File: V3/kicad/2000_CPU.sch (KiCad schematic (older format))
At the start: 21 parts, among them U2100 Z8-L180-S180-180-PQFP-80, U2101 GAL16V8, U2102 14.7456 MHz, U2103 74HCT273

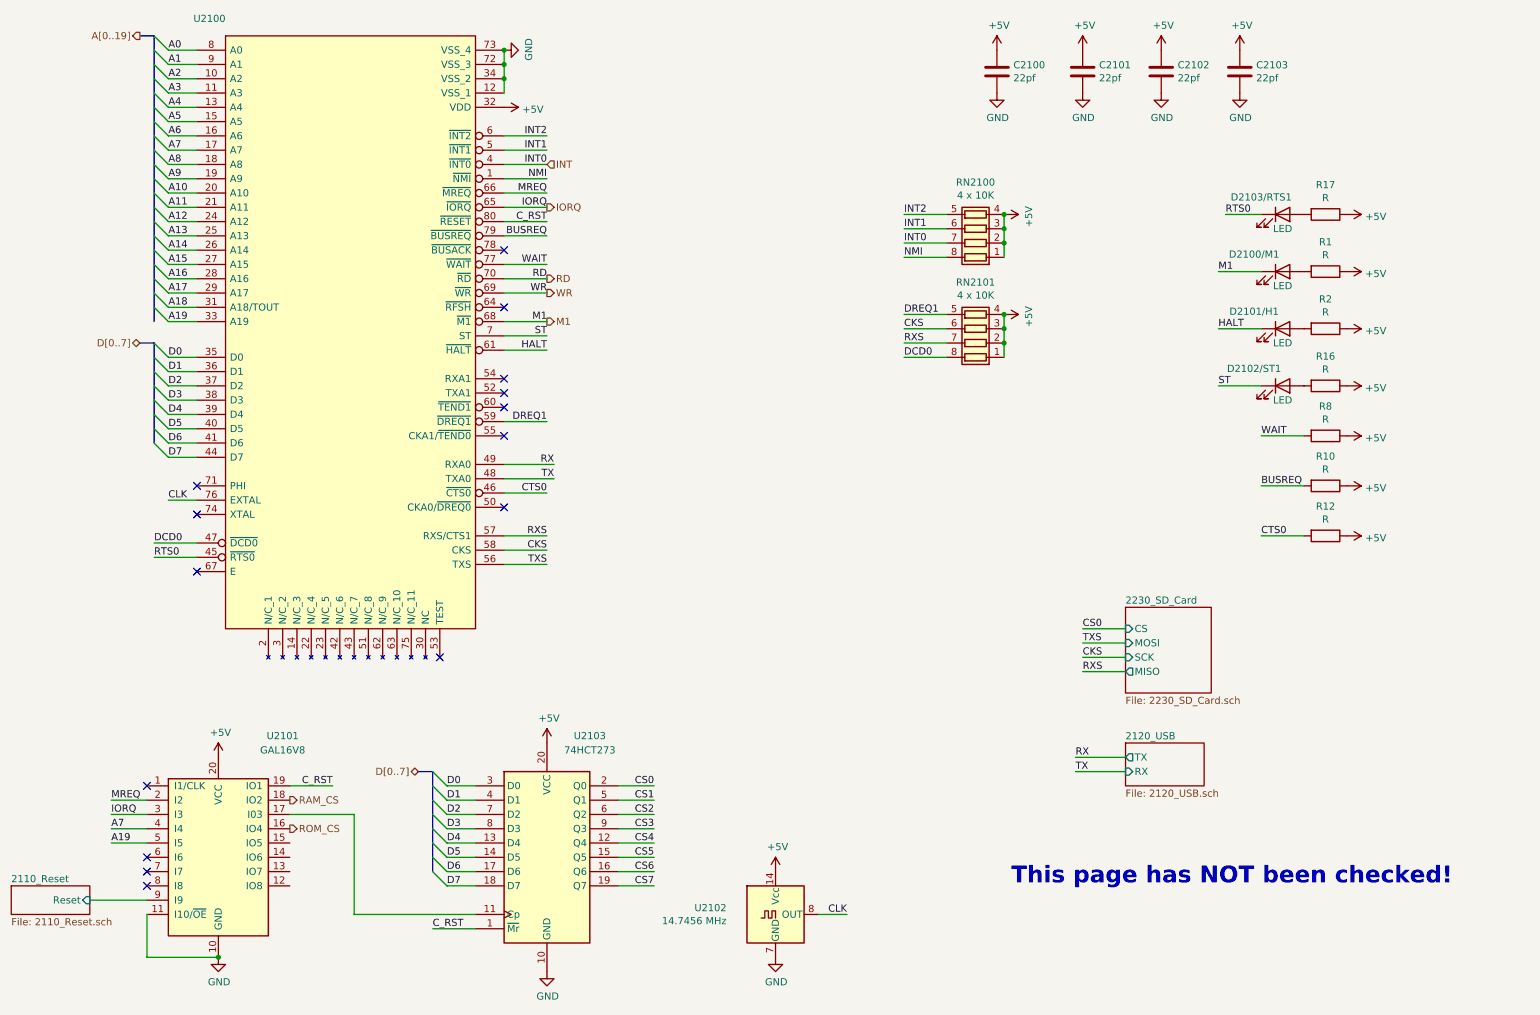
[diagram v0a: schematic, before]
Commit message: 3 1 1 m memory (#15)
* moved EEPROM files to /old

* Reworking 3.0 board

* changed footprint on RAM chip

* cleared out old memory traces

* started on rerouting

* on to autoroute

* little more cleanup

* more cleanup

* ill let the autoroute do the rest

* reroute complete

* made PQFP leads fatter

* Updated GAL logic

* Design Rule Check

* Minor pcb touch up

* gerber files

* just totally redid the whole thing

* More rearranging

* added a few caps

* Routed ROM and RAM together

* more routing

* more routes

* A lot of disorganized changes

* 3.1 CSIO SPI Bus (#9)

* Updated SPI to use CPU signals

8 bit register chip controls CS lines

* Renamed and added caps to SD page

* Cleanup

* 3.1 Resistor Replacement (#10)

* First two R arrays

* Added one more r array

* added cap for SPI FF

* Extended cpu pads (#12)

* 3.1 fix sheet hierarchy (#13)

* Fixed Schematic Heirarchy issue

* some footprints re-added to board

* Add footprints added

* Minor changes

* 3.1 redraw cpu courtyard (#14)

* moved all crtyd lines to same place in file

* Duplicate lines were causing issues

* Added pin header for SPI lines

* routed last of non-bus lines

* attempted to route memory lines

* Added new symbol and footprint

* CTS0 no longer drives an LED

* Final cleanup before memory routing

* got CTS0 and RTS mixed up

* Removed extra led from board

* Updated signature

* small changes
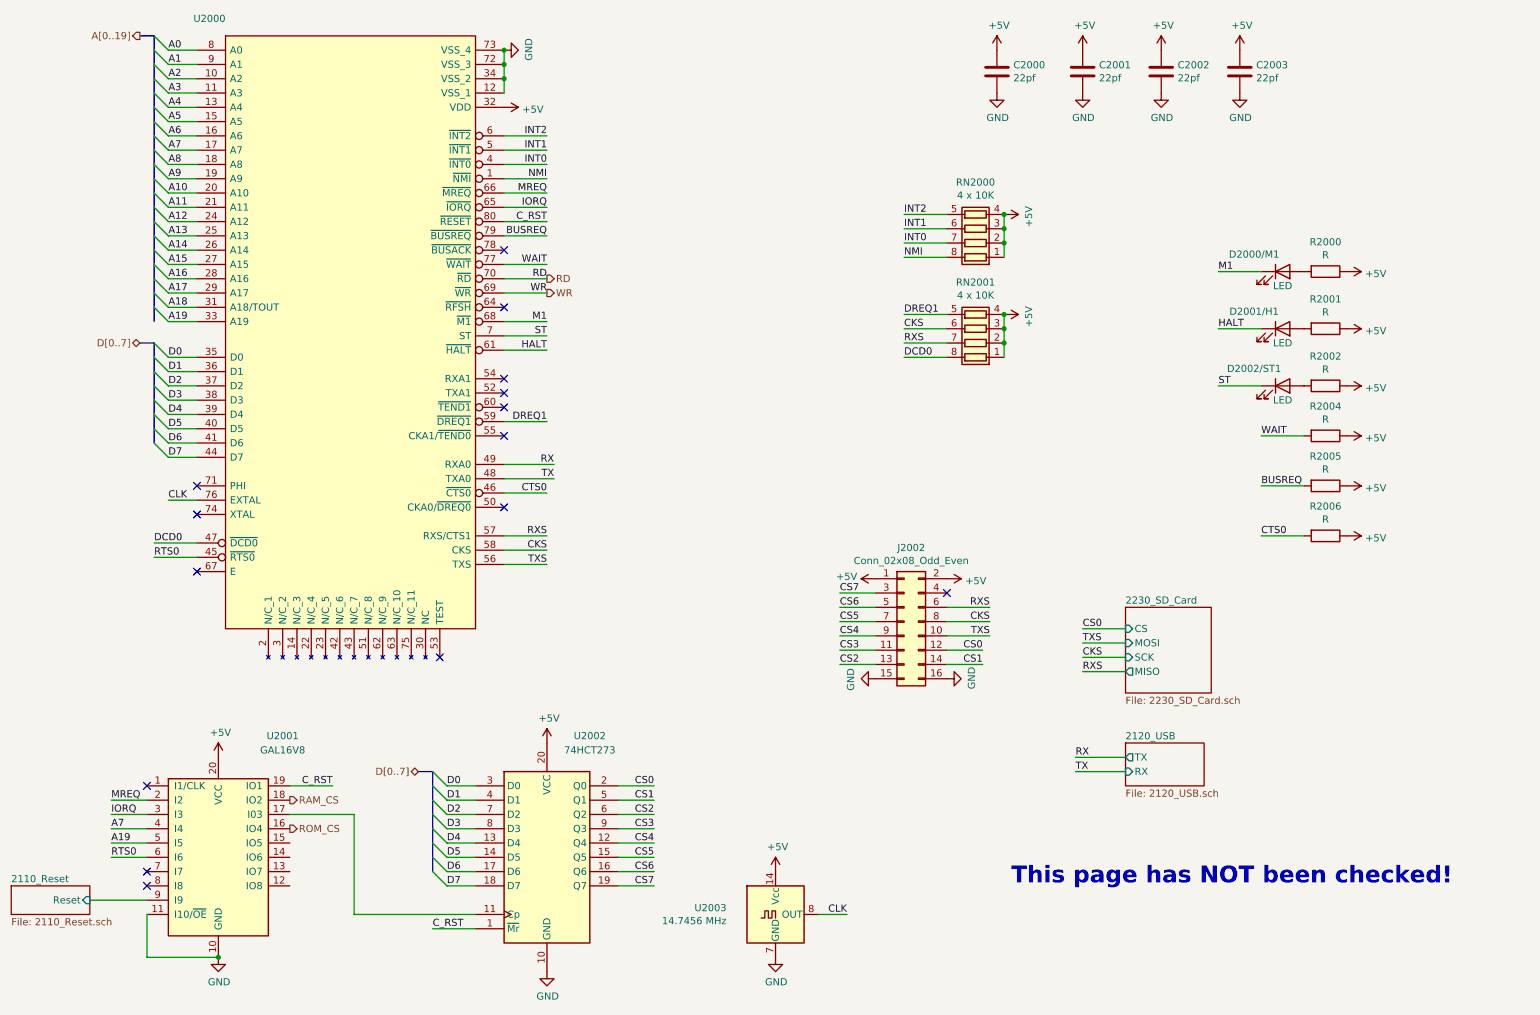
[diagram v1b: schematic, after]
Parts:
- removed D2103/RTS1: LED, LED_THT:LED_D3.0mm, symbol Device:LED
- removed R12, R17: R, Resistor_SMD:R_1206_3216Metric, symbol Device:R
- added J2002: Conn_02x08_Odd_Even, Connector_PinHeader_2.54mm:PinHeader_2x08_P2.54mm_Vertical, symbol Connector_Generic:Conn_02x08_Odd_Even
- added R2006: R, Resistor_SMD:R_1206_3216Metric, symbol Device:R
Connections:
- net +5V: now also J2002.1 (Pin_1), J2002.2 (Pin_2), R2006.1
- net CKS: now also J2002.8 (Pin_8)
- net CS0: now also J2002.12 (Pin_12)
- net CS1: now also J2002.14 (Pin_14)
- net CS2: now also J2002.13 (Pin_13)
- net CS3: now also J2002.11 (Pin_11)
- net CS4: now also J2002.9 (Pin_9)
- net CS5: now also J2002.7 (Pin_7)
- net CS6: now also J2002.5 (Pin_5)
- net CS7: now also J2002.3 (Pin_3)
- net CTS0: now also R2006.2
- net GND: now also J2002.15 (Pin_15), J2002.16 (Pin_16)
- net RTS0: now also U2101.6 (I6)
- net RXS: now also J2002.6 (Pin_6)
- net TXS: now also J2002.10 (Pin_10)
- net INT renamed INT0

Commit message: Replace chip with PLCC, strip out uncritical elements
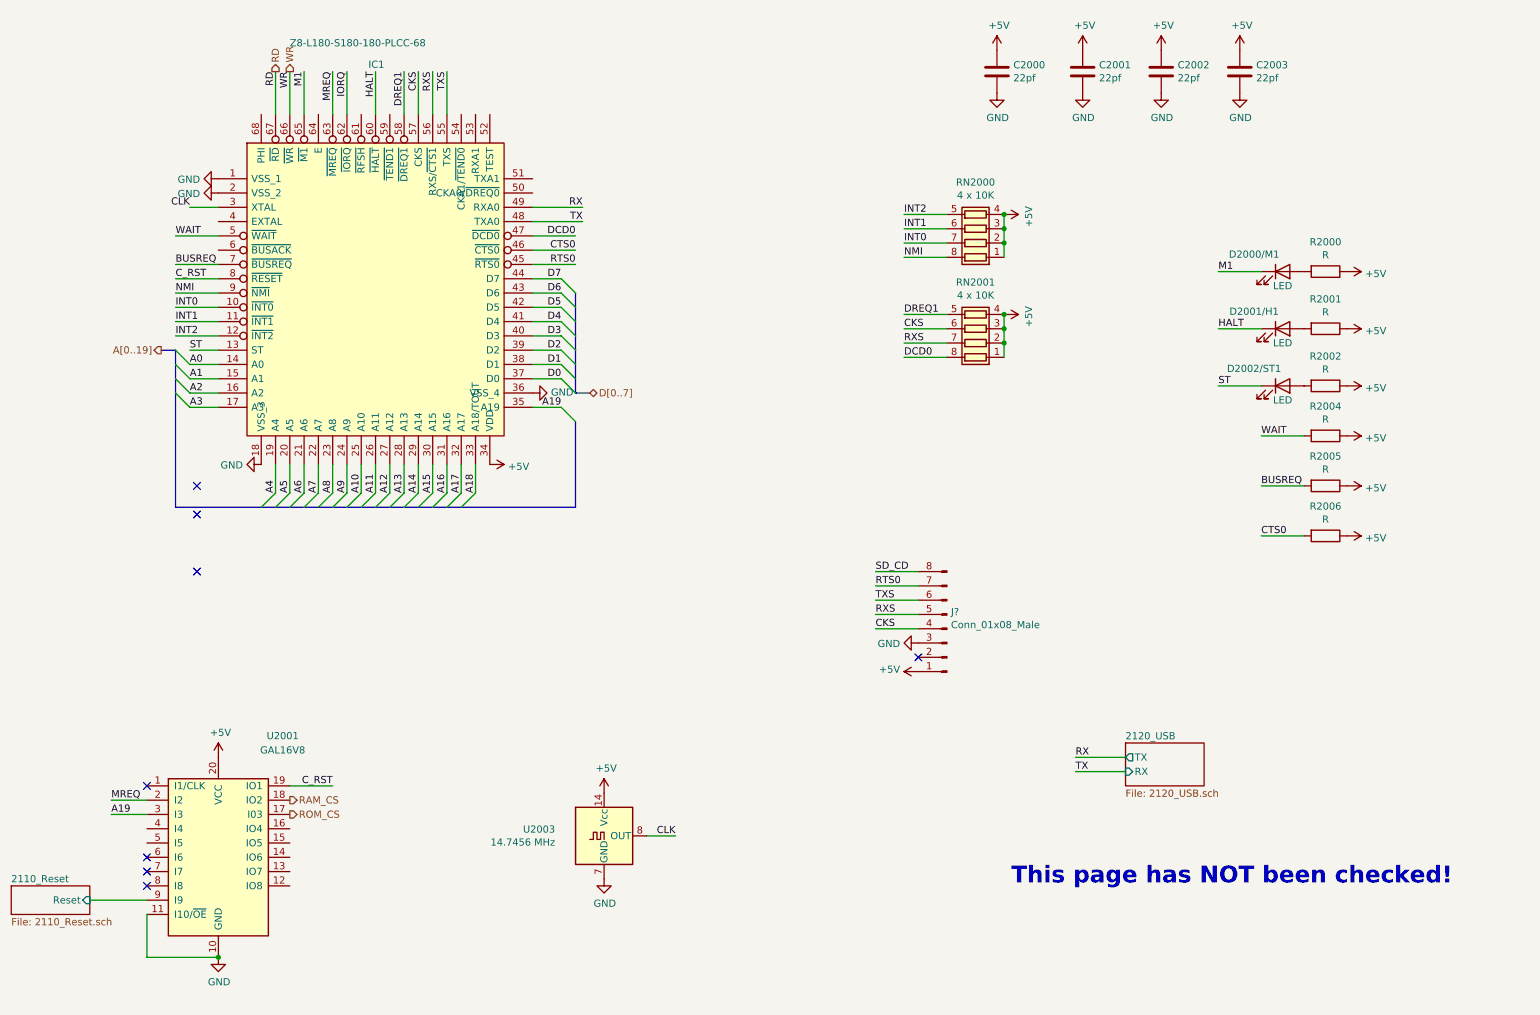
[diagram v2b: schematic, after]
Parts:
- removed J2002: Conn_02x08_Odd_Even, Connector_PinHeader_2.54mm:PinHeader_2x08_P2.54mm_Vertical, symbol Connector_Generic:Conn_02x08_Odd_Even
- removed U2100: Z8-L180-S180-180-PQFP-80, UL_Z180:Z8018008FSG, symbol Zilog_Z180:Z8-L180-S180-180-PQFP-80
- removed U2103: 74HCT273, Package_SO:SOIC-20W_7.5x12.8mm_P1.27mm, symbol 74xx:74HCT273
- added IC1: Z8-L180-S180-180-PLCC-68, Package_LCC:PLCC-68_THT-Socket, symbol Zilog_Z180:Z8-L180-S180-180-PLCC-68
- added J?: Conn_01x08_Male, symbol Connector:Conn_01x08_Male
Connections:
- net +5V: now also IC1.34 (VDD), J?.1 (Pin_1)
- net A0: now also IC1.14 (A0)
- net A1: now also IC1.15 (A1)
- net A10: now also IC1.25 (A10)
- net A11: now also IC1.26 (A11)
- net A12: now also IC1.27 (A12)
- net A13: now also IC1.28 (A13)
- net A14: now also IC1.29 (A14)
- net A15: now also IC1.30 (A15)
- net A16: now also IC1.31 (A16)
- net A17: now also IC1.32 (A17)
- net A18: now also IC1.33 (A18/TOUT)
- net A19: now also U2101.3 (I3), IC1.35 (A19); no longer U2101.5 (I5)
- net A2: now also IC1.16 (A2)
- net A3: now also IC1.17 (A3)
- net A4: now also IC1.19 (A4)
- net A5: now also IC1.20 (A5)
- net A6: now also IC1.21 (A6)
- net A7: now also IC1.22 (A7); no longer U2101.4 (I4)
- net A8: now also IC1.23 (A8)
- net A9: now also IC1.24 (A9)
- net BUSREQ: now also IC1.7 (~BUSREQ)
- net CKS: now also IC1.57 (CKS), J?.4 (Pin_4)
- net CLK: now also IC1.3 (XTAL)
- net CTS0: now also IC1.46 (~CTS0)
- net C_RST: now also IC1.8 (~RESET)
- net D0: now also IC1.37 (D0)
- net D1: now also IC1.38 (D1)
- net D2: now also IC1.39 (D2)
- net D3: now also IC1.40 (D3)
- net D4: now also IC1.41 (D4)
- net D5: now also IC1.42 (D5)
- net D6: now also IC1.43 (D6)
- net D7: now also IC1.44 (D7)
- net DCD0: now also IC1.47 (~DCD0)
- net DREQ1: now also IC1.58 (~DREQ1)
- net GND: now also IC1.1 (VSS_1), IC1.18 (VSS_3), IC1.2 (VSS_2), IC1.36 (VSS_4), J?.3 (Pin_3)
- net HALT: now also IC1.60 (~HALT)
- net INT0: now also IC1.10 (~INT0)
- net INT1: now also IC1.11 (~INT1)
- net INT2: now also IC1.12 (~INT2)
- net IORQ: now also IC1.62 (~IORQ); no longer U2101.3 (I3)
- net M1: now also IC1.65 (~M1)
- net MREQ: now also IC1.63 (~MREQ)
- net NMI: now also IC1.9 (~NMI)
- net RD: now also IC1.67 (~RD)
- net ROM_CS: now also U2101.17 (I03); no longer U2101.16 (IO4)
- net RTS0: now also IC1.45 (~RTS0), J?.7 (Pin_7); no longer U2101.6 (I6)
- net RX: now also IC1.49 (RXA0)
- net RXS: now also IC1.56 (RXS/~CTS1), J?.5 (Pin_5)
- net ST: now also IC1.13 (ST)
- net TX: now also IC1.48 (TXA0)
- net TXS: now also IC1.55 (TXS), J?.6 (Pin_6)
- net WAIT: now also IC1.5 (~WAIT)
- net WR: now also IC1.66 (~WR)
- new net SD_CD: J?.8 (Pin_8)
- no-connect marks 15 -> 8
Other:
- moved on the sheet: U2003
